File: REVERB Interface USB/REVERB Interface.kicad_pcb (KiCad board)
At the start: 2 copper layers, 90.2 x 95.9 mm, 57 parts, among them J1 RPiZeroW, J2 Iridium, J3 APRS, J4 Antenna, J6 USB_B_Micro, J7 USB, J8 USBPOGO, M1 MountingHole_Pad, M2 MountingHole_Pad, M3 MountingHole_Pad, M4 MountingHole_Pad, M5 PiMount, M6 PiMount, M7 PiMount, M8 PiMount, U1 LSM9DS1BOB, U2 MAX3232, U3 CY7C65213-28PVXI

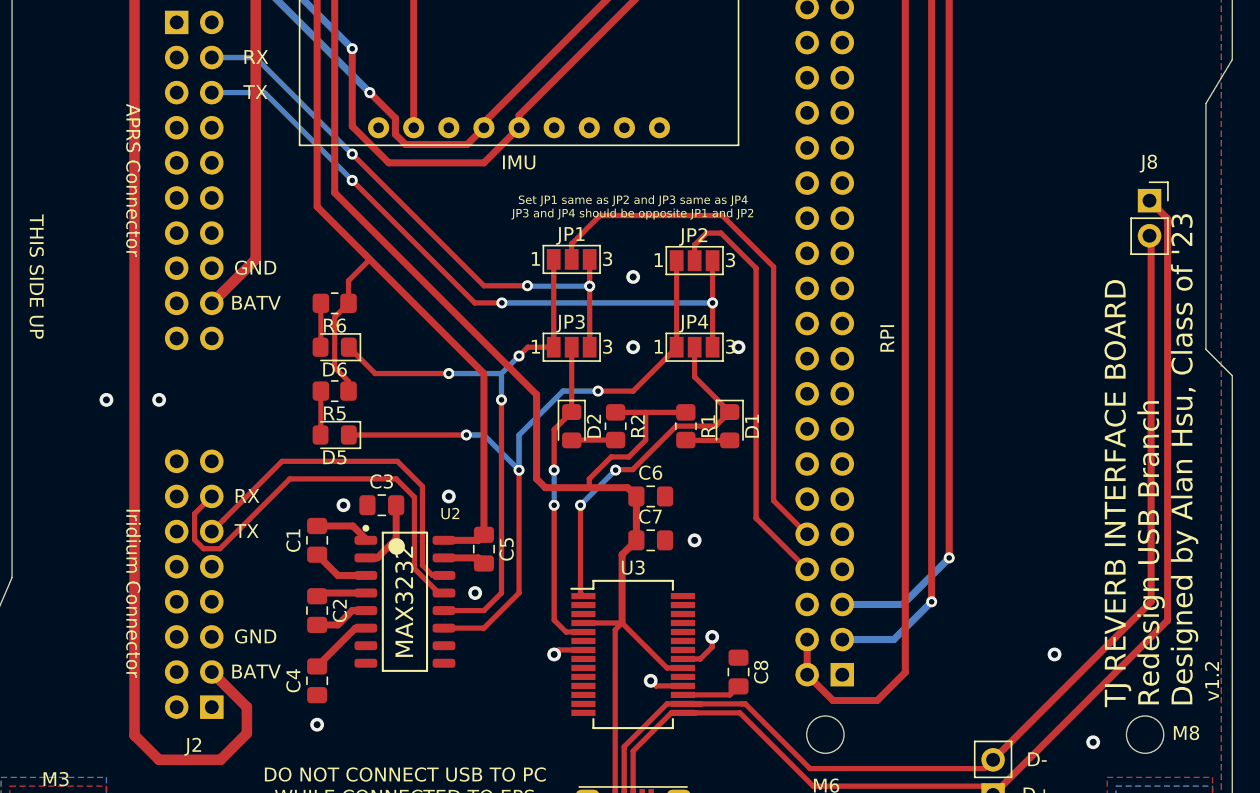
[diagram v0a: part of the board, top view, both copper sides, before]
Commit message: Improve usb branch silkscreen, push v1.3
#5 Will need to verify required clearance for connector housing later.
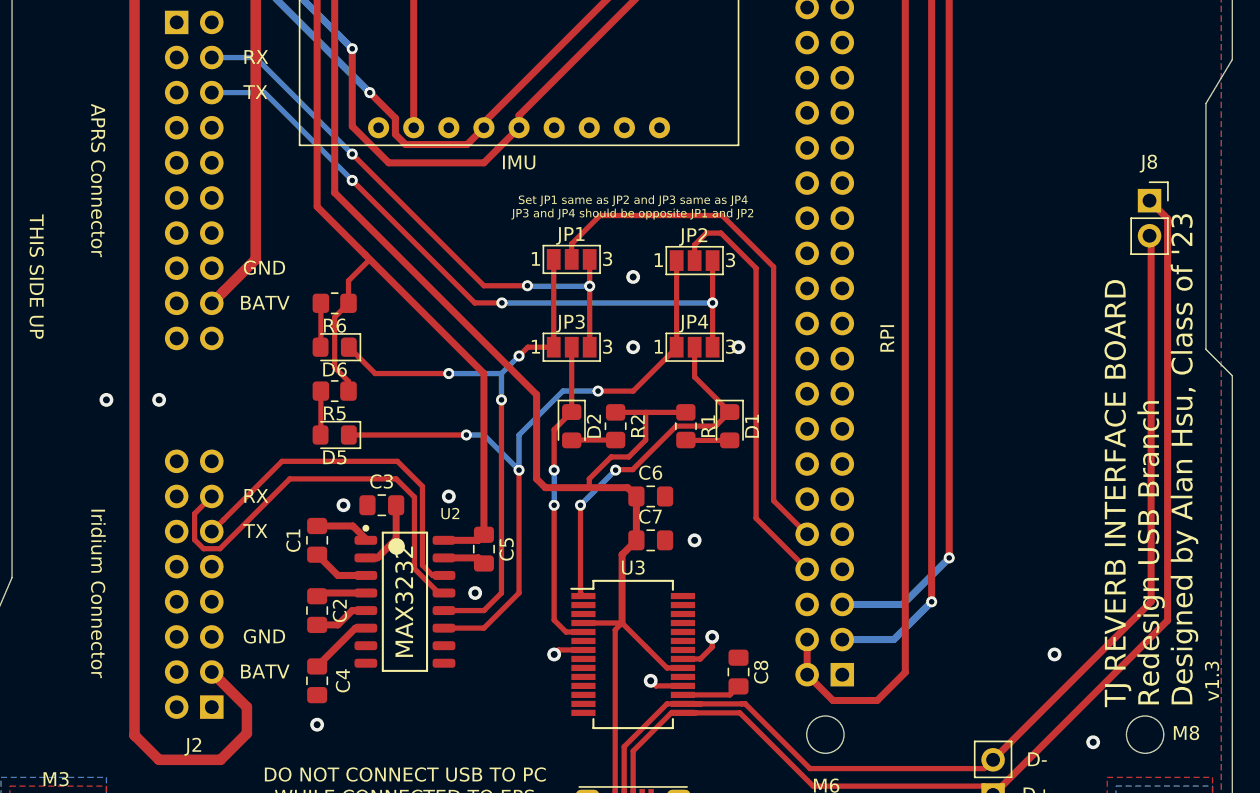
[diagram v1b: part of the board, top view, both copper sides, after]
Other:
- board text added: "v1.3"
- board text removed: "v1.2"

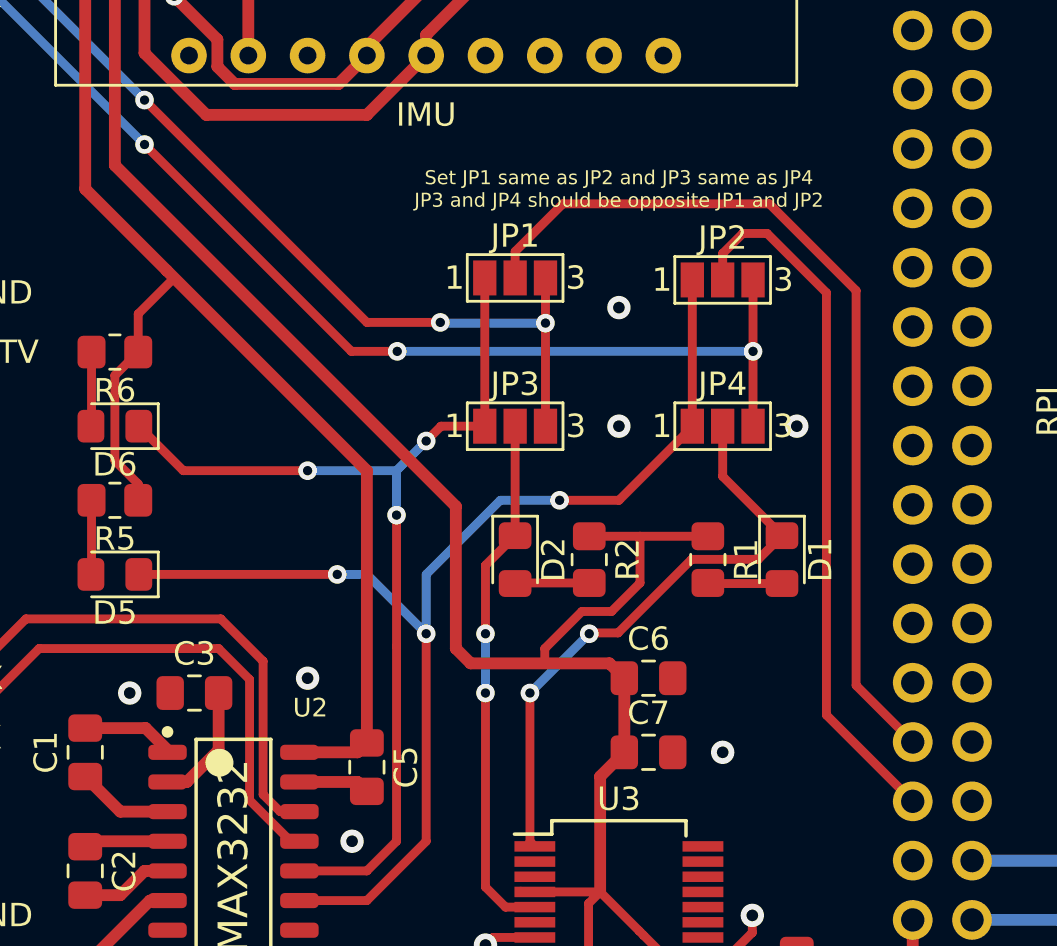
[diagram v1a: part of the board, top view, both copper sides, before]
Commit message: Add bitbang uart connections
gpio 23 and 24, #2
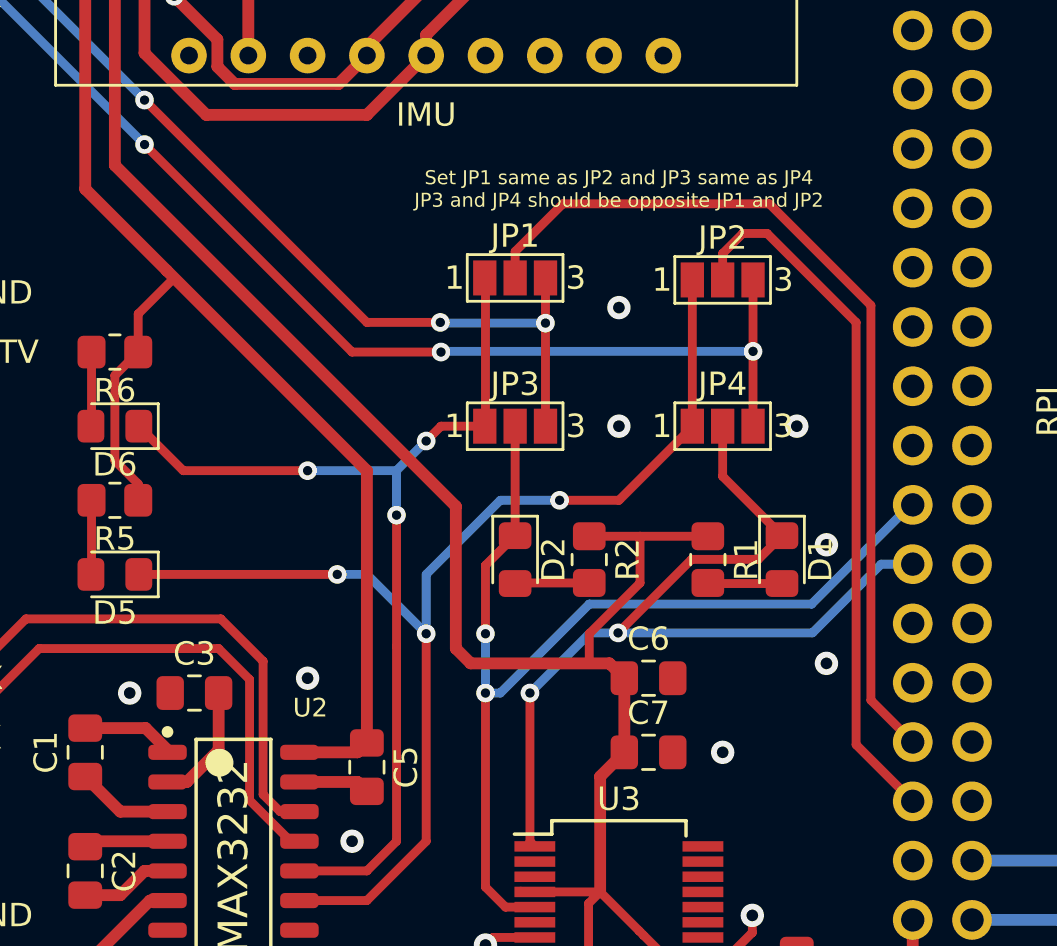
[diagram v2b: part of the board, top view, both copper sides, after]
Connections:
- J1 pad 16: (no net) -> /USBUARTTX
- J1 pad 18: (no net) -> /USBUARTRX
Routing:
- net /USBUARTRX: track 22.7 -> 44.4 mm
- net /USBUARTTX: track 26.0 -> 39.8 mm
- net GND: vias 19 -> 21

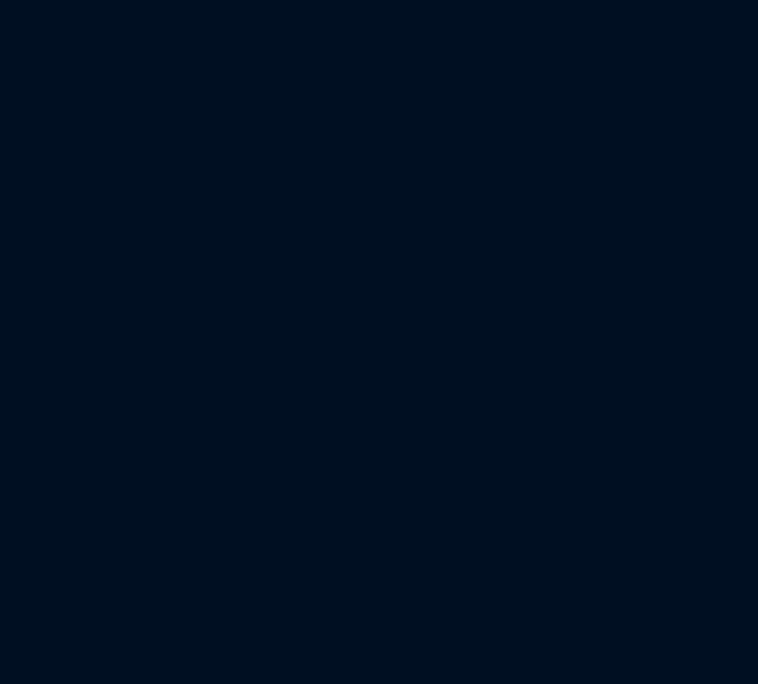
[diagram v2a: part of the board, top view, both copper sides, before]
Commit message: Add level shifters, updated sch revision numbers consistent with pcb
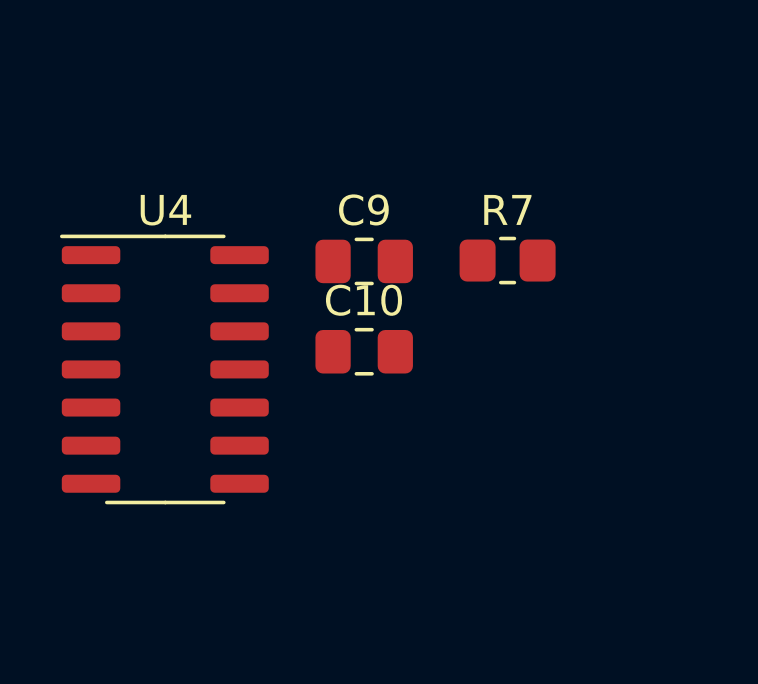
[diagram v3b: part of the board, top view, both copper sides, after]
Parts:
- added C10: 0.1uF, Capacitor_SMD:C_0805_2012Metric_Pad1.18x1.45mm_HandSolder, F.Cu at (81.3, 104.6)
- added C9: 0.1uF, Capacitor_SMD:C_0805_2012Metric_Pad1.18x1.45mm_HandSolder, F.Cu at (81.3, 101.6)
- added R7: 10K, Resistor_SMD:R_0805_2012Metric_Pad1.20x1.40mm_HandSolder, F.Cu at (86.1, 101.6)
- added U4: TXB0104D, Package_SO:SOIC-14_3.9x8.7mm_P1.27mm, F.Cu at (74.7, 105.2)
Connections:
- J1 pad 22: (no net) -> /OE
- J3 pad 4: /APRSRX -> /APRSRXSh
- J3 pad 6: /APRSTX -> /APRSTXSh

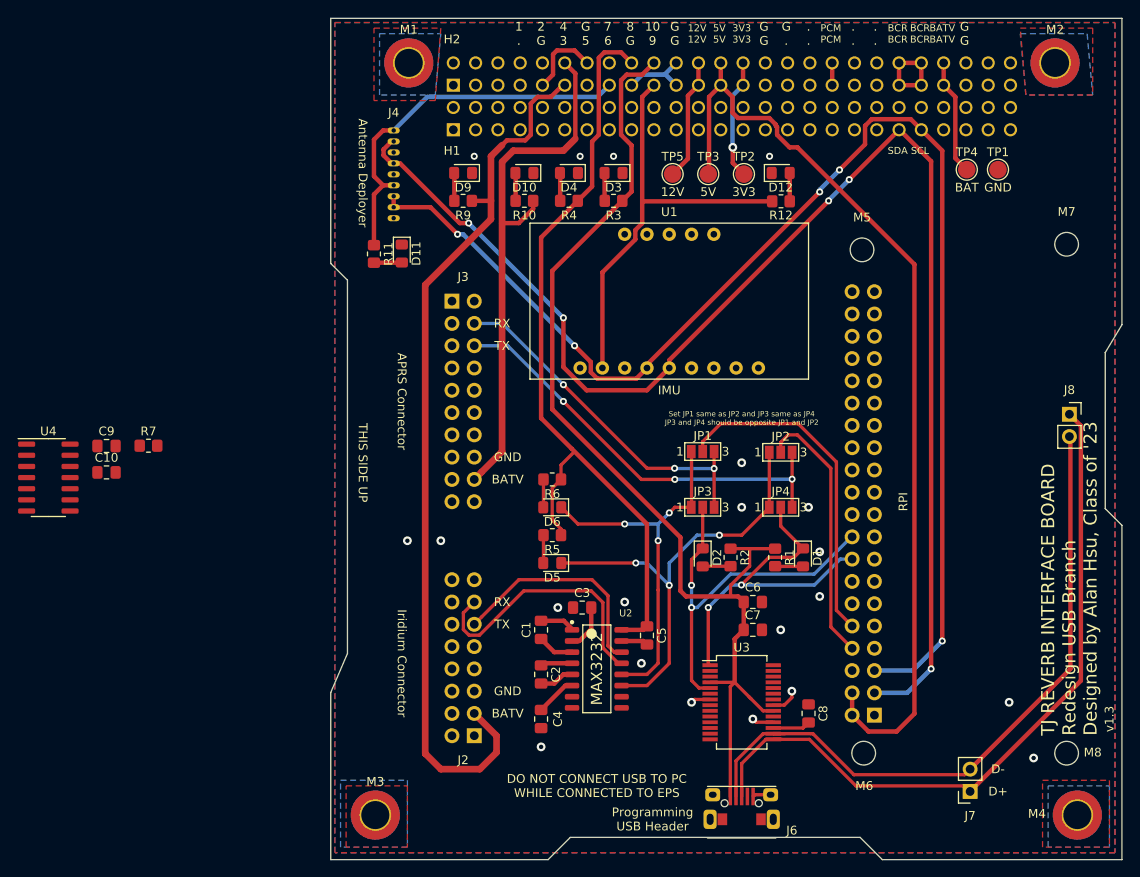
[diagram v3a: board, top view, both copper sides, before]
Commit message: add level shifter to routing
#1
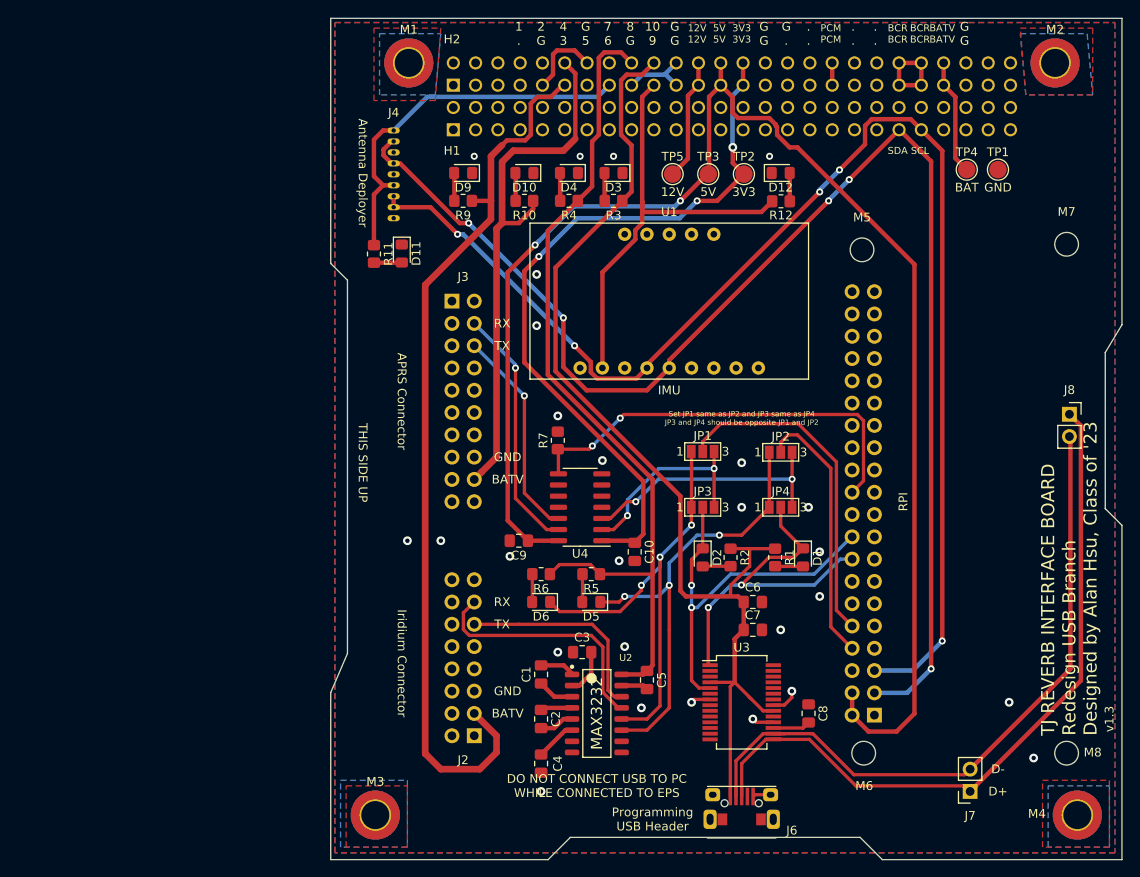
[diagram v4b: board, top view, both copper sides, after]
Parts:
- moved C10 60.9 mm to (141.5, 113.7), turned to 270 degrees
- moved U4 60.7 mm to (135.3, 108.6), turned to 180 degrees
- moved C9 48.2 mm to (128.3, 112.4), turned to 180 degrees
- moved R7 46.7 mm to (132.7, 101.0), turned to 90 degrees
- moved D6 10.9 mm to (130.8, 119.4)
- moved R6 10.9 mm to (130.8, 116.2)
- moved D5 6.29 mm to (136.5, 119.4)
- moved R5 6.29 mm to (136.5, 116.2)
- moved C5 5.08 mm to (142.9, 128.3)
- moved U2 5.08 mm to (137.2, 132.1)
- moved C1 5.08 mm to (130.8, 127.6)
- moved C2 5.08 mm to (130.8, 132.7)
- moved C3 5.08 mm to (135.5, 125.1)
- moved C4 5.08 mm to (130.8, 137.8)
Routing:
- net +3V3: track 13.7 -> 84.1 mm, vias 1 -> 3
- net +5V: track 107.9 -> 170.4 mm, vias 0 -> 2
- net /OE: track 0.00 -> 48.3 mm, vias 0 -> 2
- net /APRSRXSh: track 0.00 -> 28.2 mm, vias 0 -> 1
- net /APRSTXSh: track 0.00 -> 24.2 mm, vias 0 -> 1
- net /APRSTX: track 48.8 -> 29.8 mm, vias 3 -> 2
- net /APRSRX: track 40.5 -> 23.1 mm, vias 3 -> 2
- net /R1OUT: track 43.4 -> 52.1 mm
- net /SW8: track 91.2 -> 97.7 mm
- net /T1OUT: track 25.6 -> 23.5 mm
- net /R1IN: track 30.4 -> 28.3 mm
- net /SW9: track 49.5 -> 51.1 mm
- net GND: vias 21 -> 27

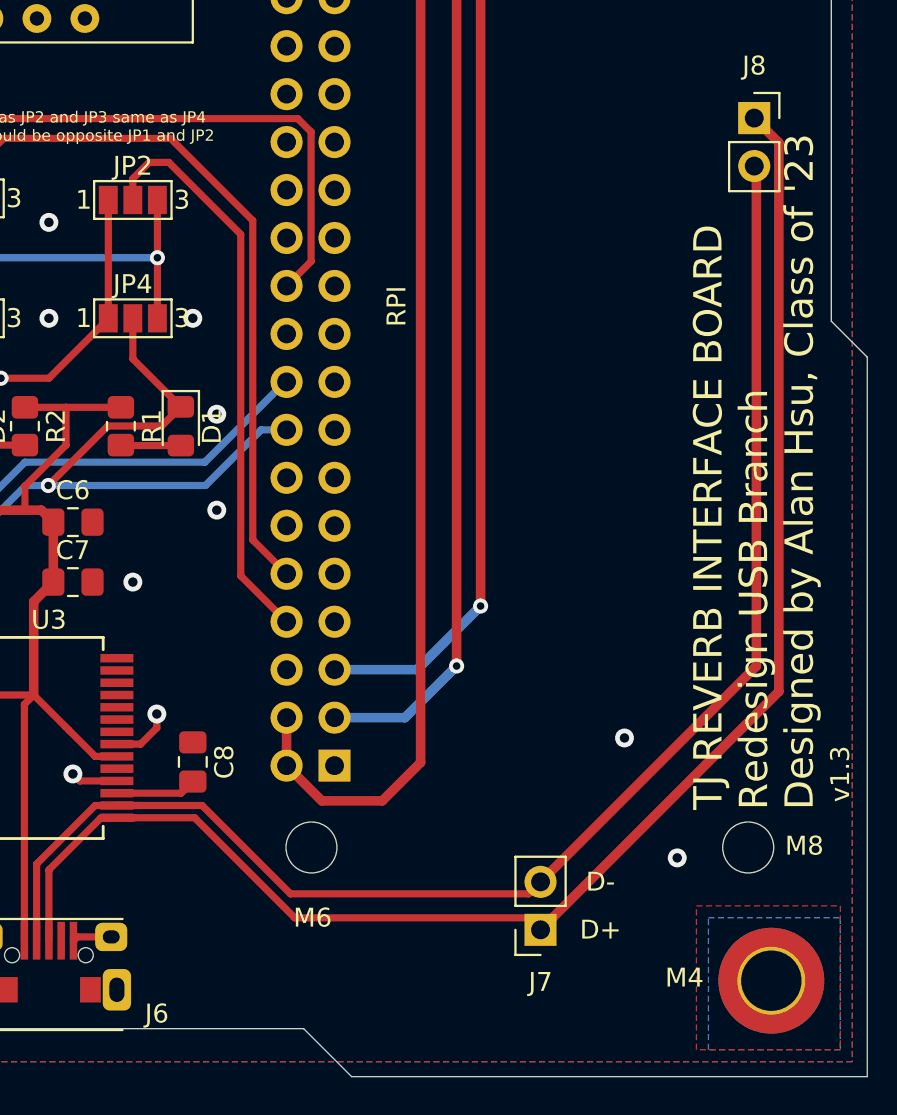
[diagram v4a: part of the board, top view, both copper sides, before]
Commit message: Fix USB header placement
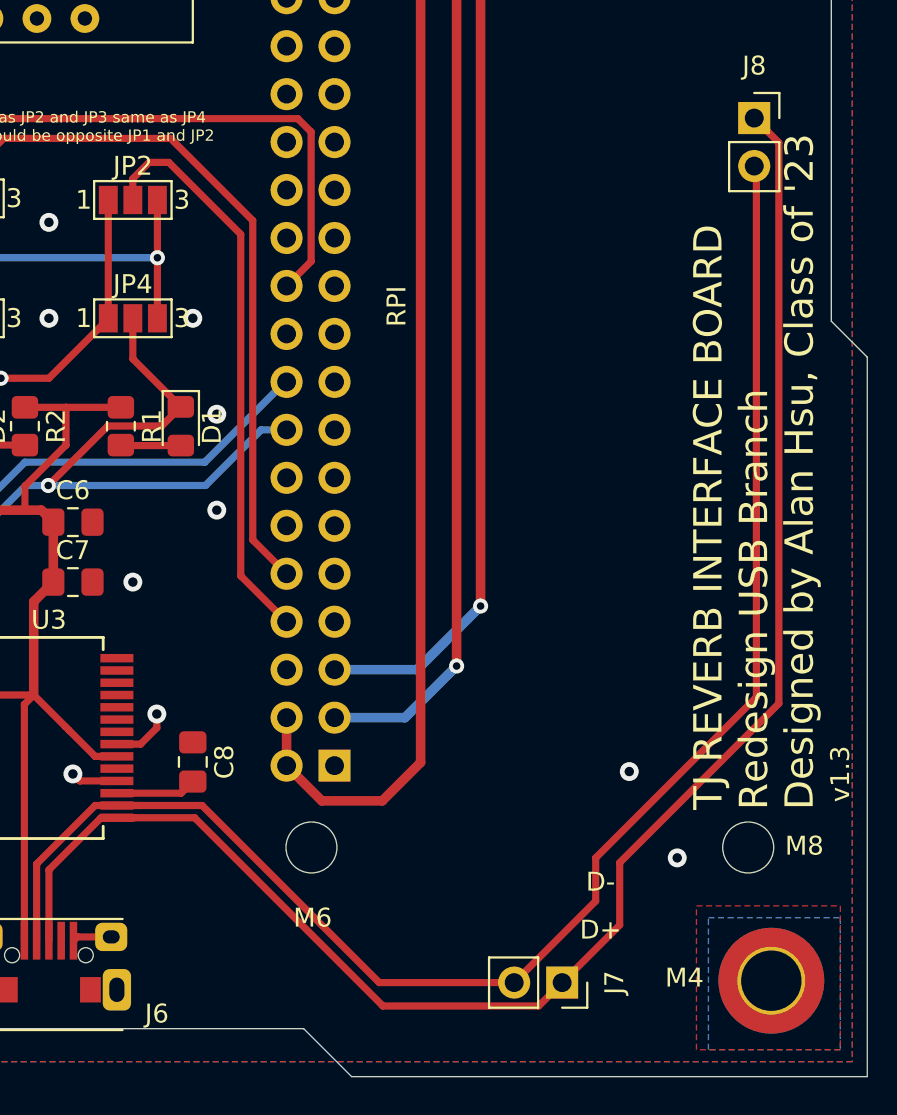
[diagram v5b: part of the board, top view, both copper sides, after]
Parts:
- moved J7 3.02 mm to (180.8, 143.8), turned to 270 degrees
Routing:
- net /D-: track 78.3 -> 84.5 mm
- net /D+: track 83.1 -> 88.7 mm
